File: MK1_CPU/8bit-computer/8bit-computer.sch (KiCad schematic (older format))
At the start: 28 parts, among them J1 Barrel_Jack_Switch, J2 USB_B-8bit-computer-rescue, U1 74LS86

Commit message: version 2.0
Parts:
- removed J1: Barrel_Jack_Switch, Connector_BarrelJack:BarrelJack_Horizontal, symbol 8bit-computer-rescue:Barrel_Jack_Switch
- removed R1, R2, R3, R4, R5, R6, R7, R8: 10K, Resistor_THT:R_Axial_DIN0207_L6.3mm_D2.5mm_P7.62mm_Horizontal, symbol Device:R
- removed R10, R11, R12, R13, R14, R15, R16, R9: 220, Resistor_THT:R_Axial_DIN0207_L6.3mm_D2.5mm_P7.62mm_Horizontal, symbol Device:R
- removed U1: 74LS86, Package_DIP:DIP-14_W7.62mm_Socket, symbol 8bit-computer-rescue:74LS86
- added C43: 10µF, Capacitor_THT:CP_Radial_D5.0mm_P2.00mm, symbol Device:CP1
- added J2: Barrel_Jack_Switch, Connector_BarrelJack:BarrelJack_Horizontal, symbol 8bit-computer-rescue:Barrel_Jack_Switch
- added RN1, RN2: 220, Resistor_THT:R_Array_SIP9, symbol Device:R_Network08
- added U1, U2: 74HCT32, Package_DIP:DIP-14_W7.62mm, symbol 8bit-computer-rescue:74HCT32
- renumbered J2 to J1
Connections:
- net labels added: A_0, A_1, A_2, A_3, A_4, A_5, A_6, A_7, BUS_0, BUS_1, BUS_2, BUS_3, BUS_4, BUS_5, BUS_6, BUS_7, CLK, CLR, IR_0, IR_1, IR_2, IR_3, IR_4, IR_5, IR_6, IR_7, ~CLK, ~CLR
- wire segments 553 -> 439
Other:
- note added: "HL"
- note added: "MI"
- note added: "RI"
- note added: "STK"
- moved on the sheet: C1, D1, D2, D3, D4, D5, D6, D7, D8, J1

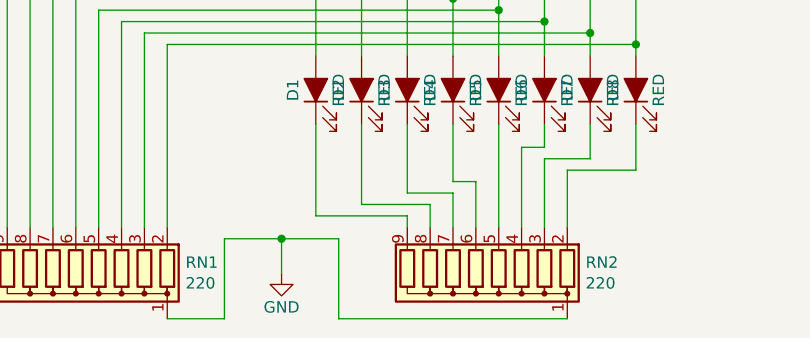
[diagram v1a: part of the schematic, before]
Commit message: resistor label update
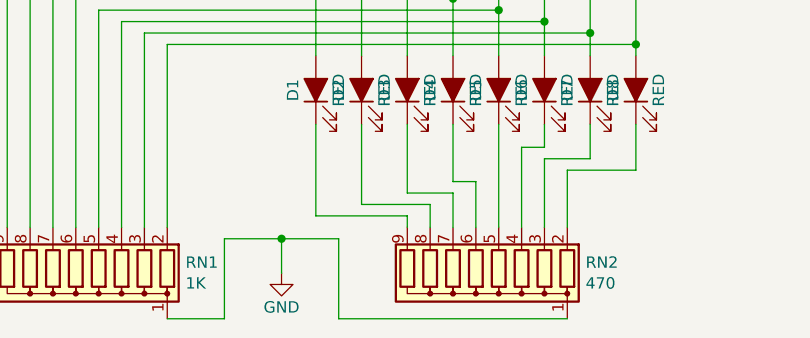
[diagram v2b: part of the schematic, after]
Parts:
- RN1: value 220 -> 1K
- RN2: value 220 -> 470
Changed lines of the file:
@@
 P 2650 10850
 F 0 "RN2" H 2170 10804 50  0000 R CNN
-F 1 "220" H 2170 10895 50  0000 R CNN
+F 1 "470" H 2170 10895 50  0000 R CNN
 F 2 "Resistor_THT:R_Array_SIP9" V 3125 10850 50  0001 C CNN
 F 3 "http://www.vishay.com/docs/31509/csc.pdf" H 2650 10850 50  0001 C CNN
@@
 P 900 10850
 F 0 "RN1" H 420 10804 50  0000 R CNN
-F 1 "220" H 420 10895 50  0000 R CNN
+F 1 "1K" H 420 10895 50  0000 R CNN
 F 2 "Resistor_THT:R_Array_SIP9" V 1375 10850 50  0001 C CNN
 F 3 "http://www.vishay.com/docs/31509/csc.pdf" H 900 10850 50  0001 C CNN

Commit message: 2.0b hardware revision
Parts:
- RN1: value 1K -> 10K
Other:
- moved on the sheet: RN1, RN2
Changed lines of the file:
@@
 L power:GND #PWR01
 U 1 1 5B60DD27
-P 1800 10850
-F 0 "#PWR01" H 1800 10600 50  0001 C CNN
-F 1 "GND" H 1800 10700 50  0000 C CNN
-F 2 "" H 1800 10850 50  0001 C CNN
-F 3 "" H 1800 10850 50  0001 C CNN
-	1    1800 10850
+P 1300 11000
+F 0 "#PWR01" H 1300 10750 50  0001 C CNN
+F 1 "GND" H 1300 10850 50  0000 C CNN
+F 2 "" H 1300 11000 50  0001 C CNN
+F 3 "" H 1300 11000 50  0001 C CNN
+	1    1300 11000
 	1    0    0    -1
 $EndComp
-Wire Wire Line
-	1800 10850 1800 10700
 Wire Wire Line
 	2350 9600 2350 9900
@@
 L power:GND #PWR03
 U 1 1 5E907257
-P 7550 9400
-F 0 "#PWR03" H 7550 9150 50  0001 C CNN
-F 1 "GND" H 7555 9227 50  0000 C CNN
-F 2 "" H 7550 9400 50  0001 C CNN
-F 3 "" H 7550 9400 50  0001 C CNN
-	1    7550 9400
+P 7550 9500
+F 0 "#PWR03" H 7550 9250 50  0001 C CNN
+F 1 "GND" H 7555 9327 50  0000 C CNN
+F 2 "" H 7550 9500 50  0001 C CNN
+F 3 "" H 7550 9500 50  0001 C CNN
+	1    7550 9500
 	1    0    0    -1
 $EndComp
@@
 Wire Wire Line
 	650  5200 950  5200
-$Comp
-L Device:R_Network08 RN2
-U 1 1 76216E60
-P 2650 10850
-F 0 "RN2" H 2170 10804 50  0000 R CNN
-F 1 "470" H 2170 10895 50  0000 R CNN
-F 2 "Resistor_THT:R_Array_SIP9" V 3125 10850 50  0001 C CNN
-F 3 "http://www.vishay.com/docs/31509/csc.pdf" H 2650 10850 50  0001 C CNN
-	1    2650 10850
-	-1   0    0    1
-$EndComp
-Wire Wire Line
-	3050 11050 2050 11050
-Wire Wire Line
-	2050 11050 2050 10700
-Wire Wire Line
-	2050 10700 1800 10700
-Wire Wire Line
-	1950 10600 2350 10600
-Wire Wire Line
-	2350 10600 2350 10650
-Wire Wire Line
-	1950 10200 1950 10600
-Wire Wire Line
-	2150 10550 2450 10550
-Wire Wire Line
-	2450 10550 2450 10650
-Wire Wire Line
-	2150 10200 2150 10550
-Wire Wire Line
-	2350 10500 2550 10500
-Wire Wire Line
-	2550 10500 2550 10650
-Wire Wire Line
-	2350 10200 2350 10500
-Wire Wire Line
-	2550 10450 2650 10450
-Wire Wire Line
-	2650 10450 2650 10650
-Wire Wire Line
-	2550 10200 2550 10450
-Wire Wire Line
-	2750 10200 2750 10650
-Wire Wire Line
-	2950 10300 2950 10200
-Wire Wire Line
-	2950 10300 2850 10300
-Wire Wire Line
-	2850 10300 2850 10650
-Wire Wire Line
-	3150 10350 2950 10350
-Wire Wire Line
-	2950 10350 2950 10650
-Wire Wire Line
-	3150 10200 3150 10350
-Wire Wire Line
-	3350 10400 3050 10400
-Wire Wire Line
-	3050 10400 3050 10650
-Wire Wire Line
-	3350 10200 3350 10400
+Wire Wire Line
+	1950 10550 2350 10550
+Wire Wire Line
+	1950 10200 1950 10550
+Wire Wire Line
+	2150 10500 2450 10500
+Wire Wire Line
+	2450 10500 2450 10550
+Wire Wire Line
+	2150 10200 2150 10500
+Wire Wire Line
+	2350 10450 2550 10450
+Wire Wire Line
+	2550 10450 2550 10550
+Wire Wire Line
+	2350 10200 2350 10450
+Wire Wire Line
+	2550 10400 2650 10400
+Wire Wire Line
+	2650 10400 2650 10550
+Wire Wire Line
+	2550 10200 2550 10400
+Wire Wire Line
+	2750 10200 2750 10550
+Wire Wire Line
+	2950 10250 2950 10200
+Wire Wire Line
+	2950 10250 2850 10250
+Wire Wire Line
+	2850 10250 2850 10550
+Wire Wire Line
+	3150 10300 2950 10300
+Wire Wire Line
+	2950 10300 2950 10550
+Wire Wire Line
+	3150 10200 3150 10300
+Wire Wire Line
+	3350 10350 3050 10350
+Wire Wire Line
+	3050 10350 3050 10550
+Wire Wire Line
+	3350 10200 3350 10350
 Wire Wire Line
 	7450 7950 7750 7950
@@
 Wire Wire Line
 	2200 8050 2950 8050
-$Comp
-L Device:R_Network08 RN1
-U 1 1 7674F9C0
-P 900 10850
-F 0 "RN1" H 420 10804 50  0000 R CNN
-F 1 "1K" H 420 10895 50  0000 R CNN
-F 2 "Resistor_THT:R_Array_SIP9" V 1375 10850 50  0001 C CNN
-F 3 "http://www.vishay.com/docs/31509/csc.pdf" H 900 10850 50  0001 C CNN
-	1    900  10850
-	-1   0    0    1
-$EndComp
-Wire Wire Line
-	1300 11050 1550 11050
-Wire Wire Line
-	1550 11050 1550 10700
-Wire Wire Line
-	1550 10700 1800 10700
-Connection ~ 1800 10700
-Wire Wire Line
-	600  9500 600  10650
-Wire Wire Line
-	700  9550 700  10650
-Wire Wire Line
-	800  9600 800  10650
-Wire Wire Line
-	900  9650 900  10650
-Wire Wire Line
-	1000 9700 1000 10650
-Wire Wire Line
-	1100 9750 1100 10650
-Wire Wire Line
-	1200 9800 1200 10650
-Wire Wire Line
-	1300 9850 1300 10650
 Text Notes 3750 2300 2    60   ~ 0
 STK
@@
 Text Label 6450 6550 2    60   ~ 0
 ~CLR
+Wire Wire Line
+	600  9500 600  10550
+Wire Wire Line
+	700  9550 700  10550
+Wire Wire Line
+	800  9600 800  10550
+Wire Wire Line
+	900  9650 900  10550
+Wire Wire Line
+	1000 9700 1000 10550
+Wire Wire Line
+	1100 9750 1100 10550
+Wire Wire Line
+	1200 9800 1200 10550
+Wire Wire Line
+	1300 9850 1300 10550
+$Comp
+L Device:R_Network08 RN1
+U 1 1 7674F9C0
+P 900 10750
+F 0 "RN1" H 420 10704 50  0000 R CNN
+F 1 "10K" H 420 10795 50  0000 R CNN
+F 2 "Resistor_THT:R_Array_SIP9" V 1375 10750 50  0001 C CNN
+F 3 "http://www.vishay.com/docs/31509/csc.pdf" H 900 10750 50  0001 C CNN
+	1    900  10750
+	-1   0    0    1
+$EndComp
+Wire Wire Line
+	1300 11000 1300 10950
+$Comp
+L Device:R_Network08 RN2
+U 1 1 76216E60
+P 2650 10750
+F 0 "RN2" H 2170 10704 50  0000 R CNN
+F 1 "470" H 2170 10795 50  0000 R CNN
+F 2 "Resistor_THT:R_Array_SIP9" V 3125 10750 50  0001 C CNN
+F 3 "http://www.vishay.com/docs/31509/csc.pdf" H 2650 10750 50  0001 C CNN
+	1    2650 10750
+	-1   0    0    1
+$EndComp
+Wire Wire Line
+	1300 10950 3050 10950
+Connection ~ 1300 10950
+Wire Wire Line
+	7550 9500 7550 9400
 $EndSCHEMATC

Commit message: revision 2.0d
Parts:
- added unit 4 of U1
- renumbered C43 to C1, C1 to C2, U1 to U2
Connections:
- net Clock/HLT: now also U1.11
- net Control logic/HL: now also U2.4; no longer U2.1
- net Control logic/RI: now also U2.1; no longer U2.12
- net Control logic/~CU_EN: now also U1.13
- net GND: now also U1.7 (GND)
- net PC Interface/HL: now also U2.5; no longer U2.2
- net PC Interface/RI: now also U2.2; no longer U2.13
- net RAM/RI: now also U2.3; no longer U2.11
- net VCC: now also U1.14 (VCC)
- net at U1.9: now also U2.6; no longer U2.3
- net Instruction register/HL renamed RAM/HL
- new net Control logic/HLT: U1.12
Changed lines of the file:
@@
 	3150 9800 3150 9900
 $Comp
-L Device:CP1 C1
+L Device:CP1 C2
 U 1 1 5B64AF9C
 P 7550 9000
-F 0 "C1" H 7575 9100 50  0000 L CNN
+F 0 "C2" H 7575 9100 50  0000 L CNN
 F 1 "10µF" H 7575 8900 50  0000 L CNN
 F 2 "Capacitor_THT:CP_Radial_D5.0mm_P2.00mm" H 7550 9000 50  0001 C CNN
@@
 F12 "IR_6" O L 950 6250 60
 F13 "IR_7" O L 950 6350 60
-F14 "~IO" I L 950 5200 60
 F15 "II" I L 950 5300 60
-F16 "HL" I L 950 5100 60
 F17 "IR_3" O L 950 5950 60
 F18 "IR_2" O L 950 5850 60
@@
 F3 "RI" O R 4150 6650 60
 F4 "~RO" O R 4150 6550 60
-F5 "~IO" O L 2950 5700 60
 F6 "~AO" O L 2950 7750 60
 F7 "~EO" O R 4150 7000 60
@@
 	1150 800  950  800
 Wire Wire Line
-	950  800  950  550
-Wire Wire Line
-	950  550  4350 550
-Wire Wire Line
-	4350 550  4350 5400
-Wire Wire Line
 	4350 5400 4150 5400
 Wire Wire Line
@@
 $Comp
 L 8bit-computer-rescue:74HCT32 U2
-U 1 1 7604CCE0
+U 2 1 7604CCE0
 P 5900 6800
 F 0 "U2" H 5900 7166 50  0000 C CNN
@@
 F 2 "Package_DIP:DIP-14_W7.62mm" H 5900 6800 50  0001 C CNN
 F 3 "" H 5900 6800 50  0001 C CNN
-	1    5900 6800
+	2    5900 6800
 	0    -1   -1   0
 $EndComp
@@
 	850  4300 950  4300
 $Comp
-L 8bit-computer-rescue:74HCT32 U1
-U 4 1 760B125A
+L 8bit-computer-rescue:74HCT32 U2
+U 1 1 760B125A
 P 5300 6850
-F 0 "U1" H 5300 7216 50  0000 C CNN
+F 0 "U2" H 5300 7216 50  0000 C CNN
 F 1 "74HCT32" H 5300 7125 50  0000 C CNN
 F 2 "Package_DIP:DIP-14_W7.62mm" H 5300 6850 50  0001 C CNN
 F 3 "" H 5300 6850 50  0001 C CNN
-	4    5300 6850
+	1    5300 6850
 	0    -1   -1   0
 $EndComp
@@
 	4250 8200 4150 8200
 Wire Wire Line
-	850  4750 850  5100
-Wire Wire Line
-	850  5100 950  5100
-Connection ~ 850  4750
-Wire Wire Line
 	950  5300 750  5300
 Wire Wire Line
@@
 Wire Wire Line
 	2300 5600 2950 5600
-Wire Wire Line
-	2950 5700 2400 5700
-Wire Wire Line
-	2400 5700 2400 7300
-Wire Wire Line
-	2400 7300 650  7300
-Wire Wire Line
-	650  7300 650  5200
-Wire Wire Line
-	650  5200 950  5200
 Wire Wire Line
 	1950 10550 2350 10550
@@
 RI
 $Comp
-L Device:CP1 C43
+L Device:CP1 C1
 U 1 1 5EB37267
 P 7200 9000
-F 0 "C43" H 7225 9100 50  0000 L CNN
+F 0 "C1" H 7225 9100 50  0000 L CNN
 F 1 "10µF" H 7225 8900 50  0000 L CNN
 F 2 "Capacitor_THT:CP_Radial_D5.0mm_P2.00mm" H 7200 9000 50  0001 C CNN
@@
 Wire Wire Line
 	7550 9500 7550 9400
+$Comp
+L 8bit-computer-rescue:74HCT32 U1
+U 4 1 5F8680A4
+P 3350 4300
+F 0 "U1" H 3350 4666 50  0000 C CNN
+F 1 "74HCT32" H 3350 4575 50  0000 C CNN
+F 2 "Package_DIP:DIP-14_W7.62mm" H 3350 4300 50  0001 C CNN
+F 3 "" H 3350 4300 50  0001 C CNN
+	4    3350 4300
+	-1   0    0    1
+$EndComp
+Wire Wire Line
+	3950 4400 4350 4400
+Wire Wire Line
+	4350 4400 4350 5400
+Wire Wire Line
+	2750 4300 2250 4300
+Wire Wire Line
+	2250 4300 2250 1450
+Wire Wire Line
+	2250 1450 950  1450
+Wire Wire Line
+	950  1450 950  800
+Wire Wire Line
+	4900 8600 4900 9000
+Wire Wire Line
+	4900 9000 2400 9000
+Wire Wire Line
+	2400 9000 2400 5750
+Wire Wire Line
+	2400 5750 2150 5750
+Wire Wire Line
+	2150 5750 2150 4650
+Wire Wire Line
+	2150 4650 4000 4650
+Wire Wire Line
+	4000 4650 4000 4200
+Wire Wire Line
+	4000 4200 3950 4200
+Connection ~ 4900 8600
 $EndSCHEMATC

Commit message: schematics cleanup
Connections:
- net Control logic/HLT renamed HLT
- net Control logic/~CU_EN renamed CU_EN
